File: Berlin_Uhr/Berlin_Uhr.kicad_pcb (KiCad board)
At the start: 2 copper layers, 100 x 130.1 mm, 62 parts, among them J1 USB_C_Receptacle_USB2.0, J2 ISP, Q1 KPS-3227, SW1 SW_Push, SW2 SW_Push, U1 DS3231M, U2 ATtiny167-SU, U3 TLC5947DAP, Y1 16MHz

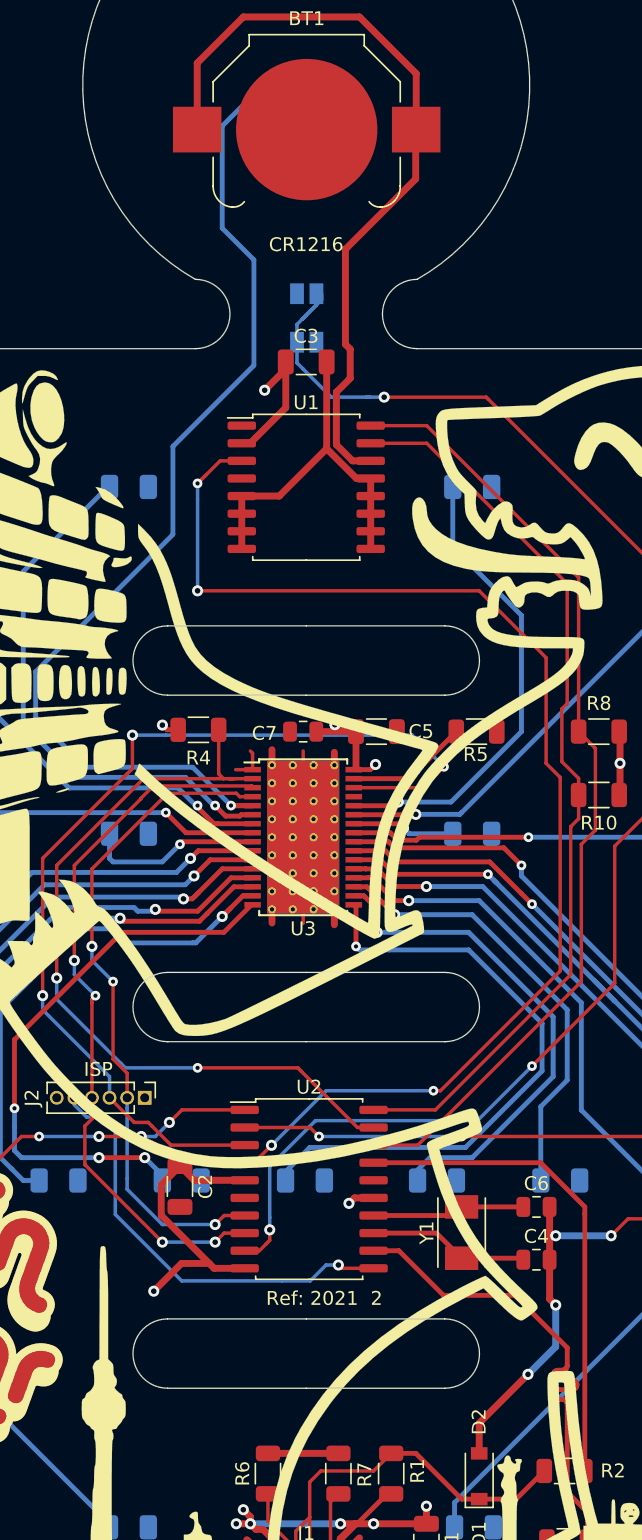
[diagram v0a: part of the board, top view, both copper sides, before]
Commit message: PCB Revision 2021 2
fixed issues:
- TLC5947 Blank pullup instead of pulldown
- KPS-3227 footprint

and some minor tweaks in routing
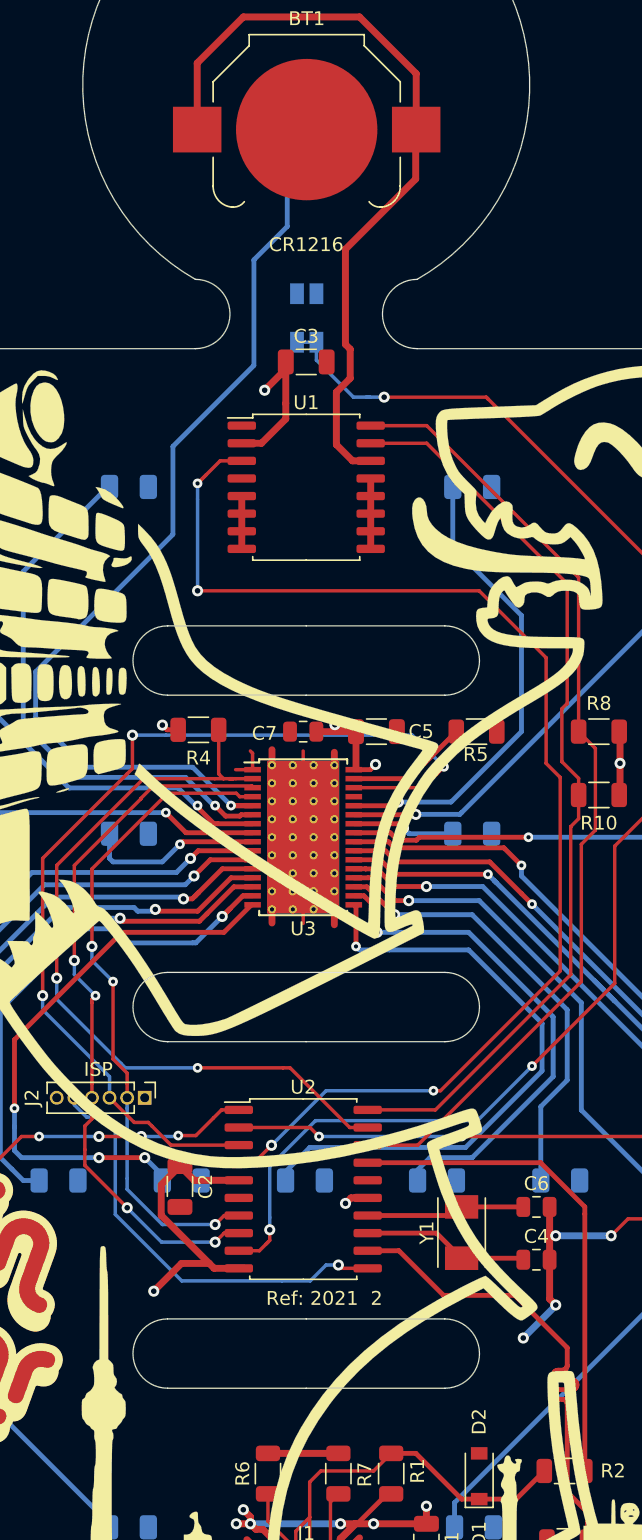
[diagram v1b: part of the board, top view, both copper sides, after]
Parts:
- R9: value 2k -> 51k
- moved U2 0.43 mm to (144.8, 120.6)
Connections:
- Q1 pad 2: Net-(Q1-Pad2) -> +5V
- Q1 pad 3: +5V -> Net-(Q1-Pad3)
- Q1 pad 4: Net-(Q1-Pad2) -> Net-(Q1-Pad3)
- R9 pad 1: Net-(Q1-Pad2) -> Net-(Q1-Pad3)
- U2 pad 9: Net-(Q1-Pad2) -> Net-(Q1-Pad3)
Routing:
- net Net-(Q1-Pad2): track 110.0 -> 0.00 mm, vias 3 -> 0
- net Net-(Q1-Pad3): track 0.00 -> 103.0 mm, vias 0 -> 3
- net GND: track 130.0 -> 102.5 mm
- net Net-(D3-Pad1): track 76.0 -> 73.0 mm
- net +5V: track 76.9 -> 78.6 mm
- net Net-(R4-Pad2): track 57.4 -> 56.6 mm

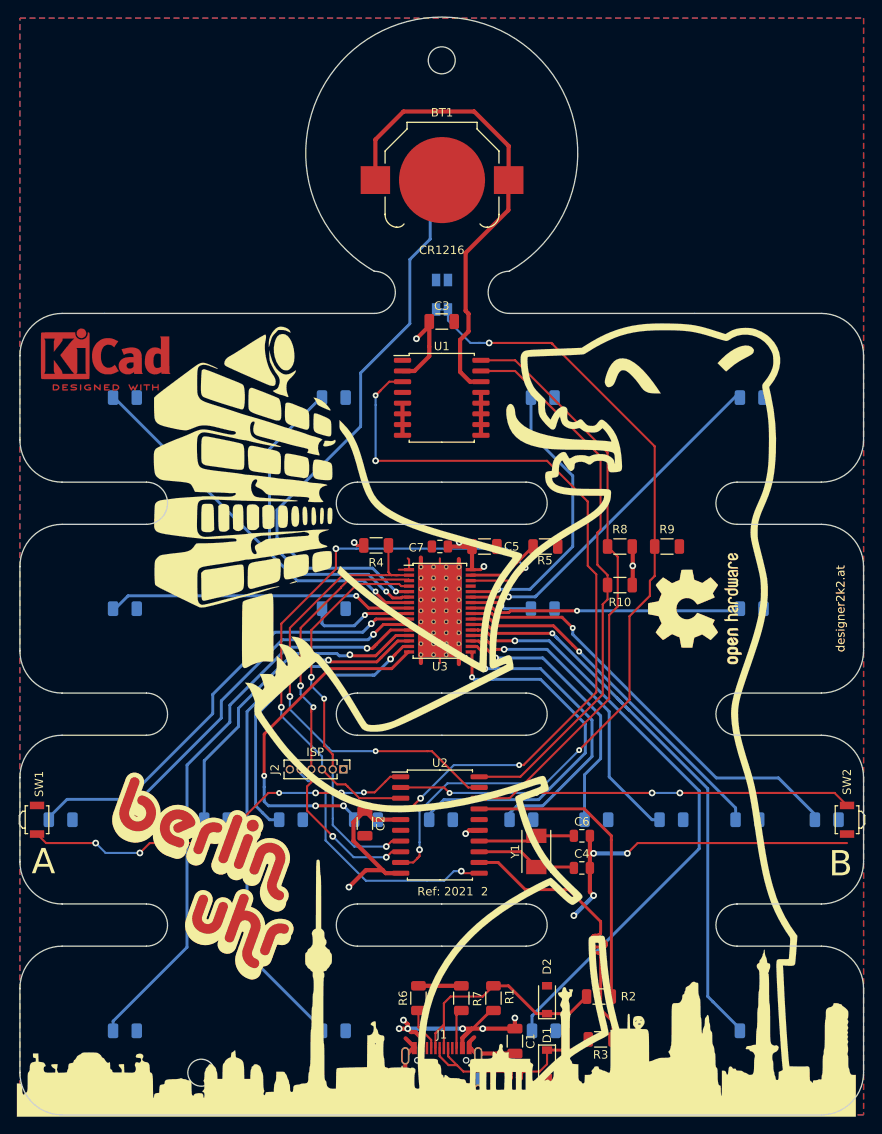
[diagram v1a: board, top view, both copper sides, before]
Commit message: PCB Update
bugfix in footprint
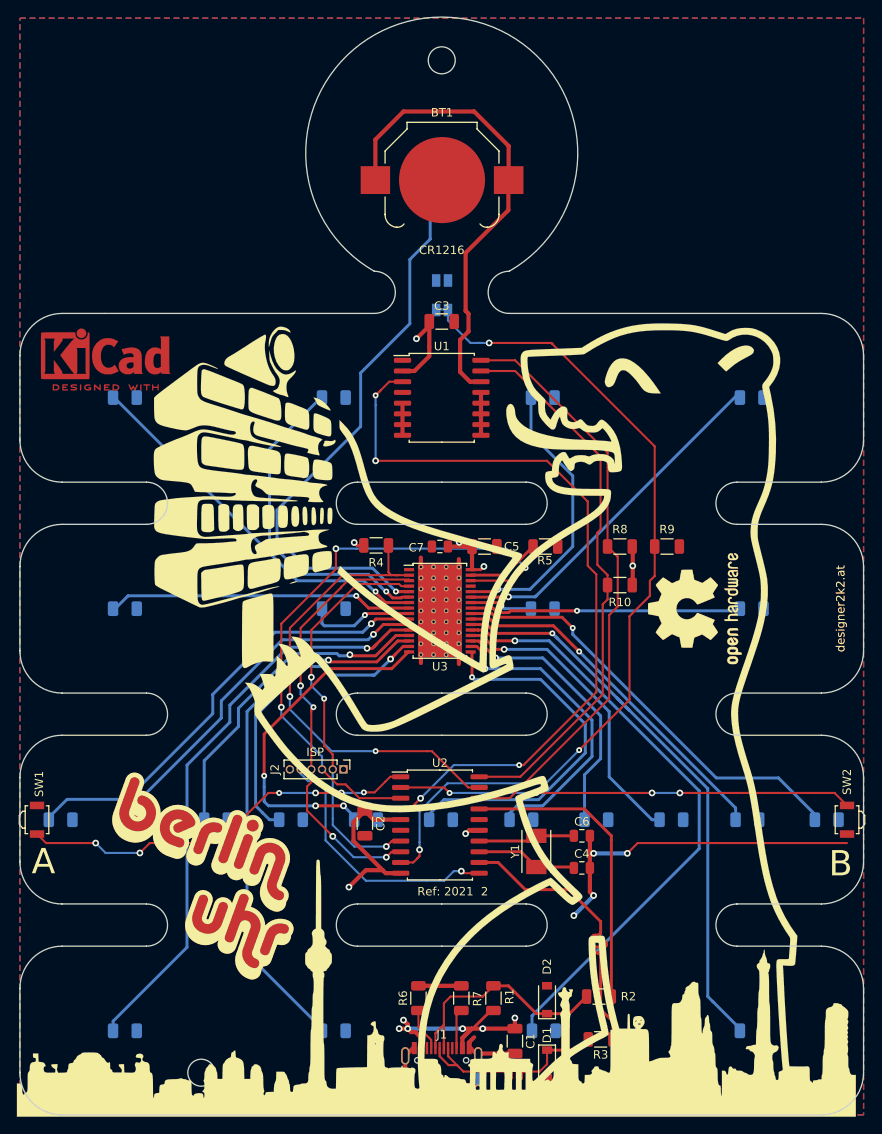
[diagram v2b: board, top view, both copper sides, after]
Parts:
- Q1: footprint LED_SMD:LED_RGB_1210 -> Berlin_Uhr:Kingbright_KPS-3227
- moved Q1 0.06 mm to (145.0, 57.8), turned to 180 degrees
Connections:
- J1 pad A8: Net-(J1-PadA8) -> unconnected-(J1-PadA8)
- J1 pad B8: Net-(J1-PadB8) -> unconnected-(J1-PadB8)
- Q1 pad 2: +5V -> Net-(Q1-Pad2)
- Q1 pad 3: Net-(Q1-Pad3) -> +5V
- Q1 pad 4: Net-(Q1-Pad3) -> Net-(Q1-Pad2)
- R9 pad 1: Net-(Q1-Pad3) -> Net-(Q1-Pad2)
- U1 pad 1: Net-(U1-Pad1) -> unconnected-(U1-Pad1)
- U1 pad 4: Net-(U1-Pad4) -> unconnected-(U1-Pad4)
- U2 pad 9: Net-(Q1-Pad3) -> Net-(Q1-Pad2)
- U3 pad 29: Net-(U3-Pad29) -> unconnected-(U3-Pad29)
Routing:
- net Net-(Q1-Pad2): track 0.00 -> 103.0 mm, vias 0 -> 3
- net Net-(Q1-Pad3): track 103.0 -> 0.00 mm, vias 3 -> 0
- net GND: track 102.5 -> 85.8 mm
- net Net-(D9-Pad1): track 45.5 -> 44.4 mm
- net Net-(D8-Pad1): track 54.7 -> 53.8 mm
- net Net-(D18-Pad1): track 36.6 -> 36.0 mm
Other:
- net class Default removed

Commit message: Switch KPS-3227 to native KiCad part.
KiCad 6.0.2 fixed the KPS-3227 Footprint, now using the build in one.
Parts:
- Q1: footprint Berlin_Uhr:Kingbright_KPS-3227 -> OptoDevice:Kingbright_KPS-3227
